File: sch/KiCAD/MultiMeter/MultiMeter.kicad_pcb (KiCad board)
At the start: 2 copper layers, 31.1 x 40.6 mm, 17 parts

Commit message: 回路図データ修正
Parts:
- removed Boost, OilPress: PinHeader_1x03_P2.54mm_Vertical, Connector_PinHeader_2.54mm:PinHeader_1x03_P2.54mm_Vertical
- removed OilTemp, WaterTemp: PinHeader_1x02_P2.54mm_Vertical, Connector_PinHeader_2.54mm:PinHeader_1x02_P2.54mm_Vertical
- removed Speed, Tacho: Pin_D1.2mm_L11.3mm_W3.0mm_Flat, Connector_Pin:Pin_D1.2mm_L11.3mm_W3.0mm_Flat
- added J1: Conn_01x02_Male, Connector_Molex:Molex_SPOX_5267-02A_1x02_P2.50mm_Vertical, F.Cu at (64.4, 65.4)
- added J2: Conn_01x02_Male, Connector_Molex:Molex_SPOX_5267-02A_1x02_P2.50mm_Vertical, F.Cu at (64.4, 56.5)
- added J3: Conn_01x03_Male, Connector_Molex:Molex_SPOX_5267-03A_1x03_P2.50mm_Vertical, F.Cu at (64.4, 45.1)
- added J4: Conn_01x03_Male, Connector_Molex:Molex_SPOX_5267-03A_1x03_P2.50mm_Vertical, F.Cu at (64.4, 33.7)
- added J5: Conn_01x02_Female, Connector_Molex:Molex_KK-254_AE-6410-02A_1x02_P2.54mm_Vertical, F.Cu at (64.8, 26.0)
- A1: value Arduino_Nano -> Arduino_Nano_v3.x
- C1, C2: value C_Rect_L4.6mm_W2.0mm_P2.50mm_MKS02_FKP02 -> C
- D1, D2, D3, D4: value D_T-1_P10.16mm_Horizontal -> 1N4148; footprint Diode_THT:D_T-1_P10.16mm_Horizontal -> Diode_THT:D_DO-35_SOD27_P7.62mm_Horizontal
- R1, R2, R3, R4: value R_Axial_DIN0207_L6.3mm_D2.5mm_P10.16mm_Horizontal -> R; footprint Resistor_THT:R_Axial_DIN0207_L6.3mm_D2.5mm_P10.16mm_Horizontal -> Resistor_THT:R_Axial_DIN0204_L3.6mm_D1.6mm_P7.62mm_Horizontal
- moved A1 55.7 mm to (42.5, 26.0), turned to 0 degrees
- moved R3 47.7 mm to (46.4, 25.4), turned to 0 degrees
- moved R4 40.3 mm to (46.4, 27.9), turned to 0 degrees
- moved D2 34.6 mm to (48.9, 38.1)
- moved C1 34.3 mm to (45.7, 55.2), turned to 0 degrees
- moved C2 34.1 mm to (52.1, 55.2)
- moved D1 29.9 mm to (48.9, 48.9), turned to 90 degrees
- moved D3 29.0 mm to (53.3, 48.9), turned to 90 degrees
- moved R1 23.8 mm to (54.0, 61.6), turned to 180 degrees
- moved D4 22.7 mm to (53.3, 38.1)
- moved R2 17.2 mm to (54.0, 59.1), turned to 180 degrees
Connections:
- A1 pad 1: (no net) -> unconnected-(A1-Pad1)
- A1 pad 10: (no net) -> unconnected-(A1-Pad10)
- A1 pad 11: (no net) -> unconnected-(A1-Pad11)
- A1 pad 12: (no net) -> unconnected-(A1-Pad12)
- A1 pad 13: (no net) -> unconnected-(A1-Pad13)
- A1 pad 14: (no net) -> unconnected-(A1-Pad14)
- A1 pad 15: (no net) -> unconnected-(A1-Pad15)
- A1 pad 16: (no net) -> unconnected-(A1-Pad16)
- A1 pad 17: (no net) -> unconnected-(A1-Pad17)
- A1 pad 18: (no net) -> unconnected-(A1-Pad18)
- A1 pad 19: (no net) -> unconnected-(A1-Pad19)
- A1 pad 2: (no net) -> unconnected-(A1-Pad2)
- A1 pad 20: (no net) -> Net-(A1-Pad20)
- A1 pad 21: (no net) -> Net-(A1-Pad21)
- A1 pad 22: (no net) -> Net-(A1-Pad22)
- A1 pad 23: (no net) -> Net-(A1-Pad23)
- A1 pad 24: (no net) -> unconnected-(A1-Pad24)
- A1 pad 25: (no net) -> unconnected-(A1-Pad25)
- A1 pad 26: (no net) -> unconnected-(A1-Pad26)
- A1 pad 27: (no net) -> Net-(A1-Pad27)
- A1 pad 28: (no net) -> unconnected-(A1-Pad28)
- A1 pad 29: (no net) -> Net-(A1-Pad29)
- A1 pad 3: (no net) -> unconnected-(A1-Pad3)
- A1 pad 30: (no net) -> unconnected-(A1-Pad30)
- A1 pad 4: (no net) -> Net-(A1-Pad29)
- A1 pad 5: (no net) -> Net-(A1-Pad5)
- A1 pad 6: (no net) -> Net-(A1-Pad6)
- A1 pad 7: (no net) -> unconnected-(A1-Pad7)
- A1 pad 8: (no net) -> unconnected-(A1-Pad8)
- A1 pad 9: (no net) -> unconnected-(A1-Pad9)
- C1 pad 1: (no net) -> Net-(A1-Pad5)
- C1 pad 2: (no net) -> Net-(A1-Pad29)
- C2 pad 1: (no net) -> Net-(A1-Pad6)
- C2 pad 2: (no net) -> Net-(A1-Pad29)
- D1 pad 1: (no net) -> Net-(A1-Pad5)
- D1 pad 2: (no net) -> Net-(A1-Pad29)
- D2 pad 1: (no net) -> Net-(A1-Pad27)
- D2 pad 2: (no net) -> Net-(A1-Pad5)
- D3 pad 1: (no net) -> Net-(A1-Pad6)
- D3 pad 2: (no net) -> Net-(A1-Pad29)
- D4 pad 1: (no net) -> Net-(A1-Pad27)
- D4 pad 2: (no net) -> Net-(A1-Pad6)
- R1 pad 1: (no net) -> Net-(A1-Pad20)
- R1 pad 2: (no net) -> Net-(A1-Pad29)
- R2 pad 1: (no net) -> Net-(A1-Pad21)
- R2 pad 2: (no net) -> Net-(A1-Pad29)
- R3 pad 1: (no net) -> Net-(A1-Pad5)
- R3 pad 2: (no net) -> Net-(J5-Pad1)
- R4 pad 1: (no net) -> Net-(A1-Pad6)
- R4 pad 2: (no net) -> Net-(J5-Pad2)
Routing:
- net (no net): track 290.2 -> 0.00 mm
- net Net-(A1-Pad29): track 0.00 -> 86.6 mm
- net Net-(A1-Pad27): track 0.00 -> 59.7 mm
- net Net-(A1-Pad6): track 0.00 -> 54.2 mm
- net Net-(A1-Pad5): track 0.00 -> 42.7 mm
- net Net-(A1-Pad20): track 0.00 -> 29.8 mm
- net Net-(A1-Pad21): track 0.00 -> 24.1 mm
- net Net-(A1-Pad23): track 0.00 -> 13.5 mm
- net Net-(J5-Pad1): track 0.00 -> 11.6 mm
- net Net-(J5-Pad2): track 0.00 -> 11.4 mm
- net Net-(A1-Pad22): track 0.00 -> 7.16 mm
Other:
- board size 31.1 x 40.6 mm -> 29.8 x 52.7 mm
- board text added: "2022/09/13"
- board text added: "Boost"
- board text added: "Oil.P"
- board text added: "Oil.T"
- board text added: "Water"
- board text removed: "2022/08/18"
- board text removed: "USB"

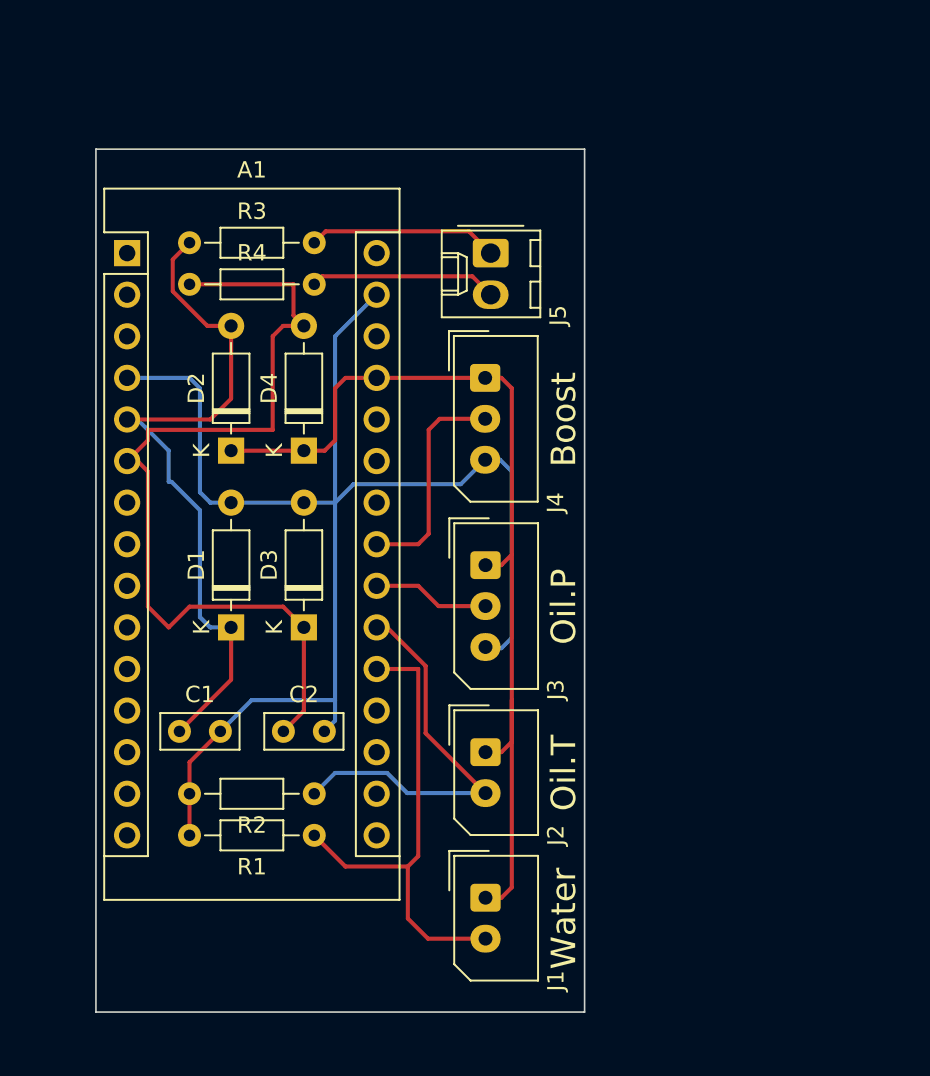
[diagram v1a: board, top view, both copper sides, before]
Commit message: デバック用PADを追加
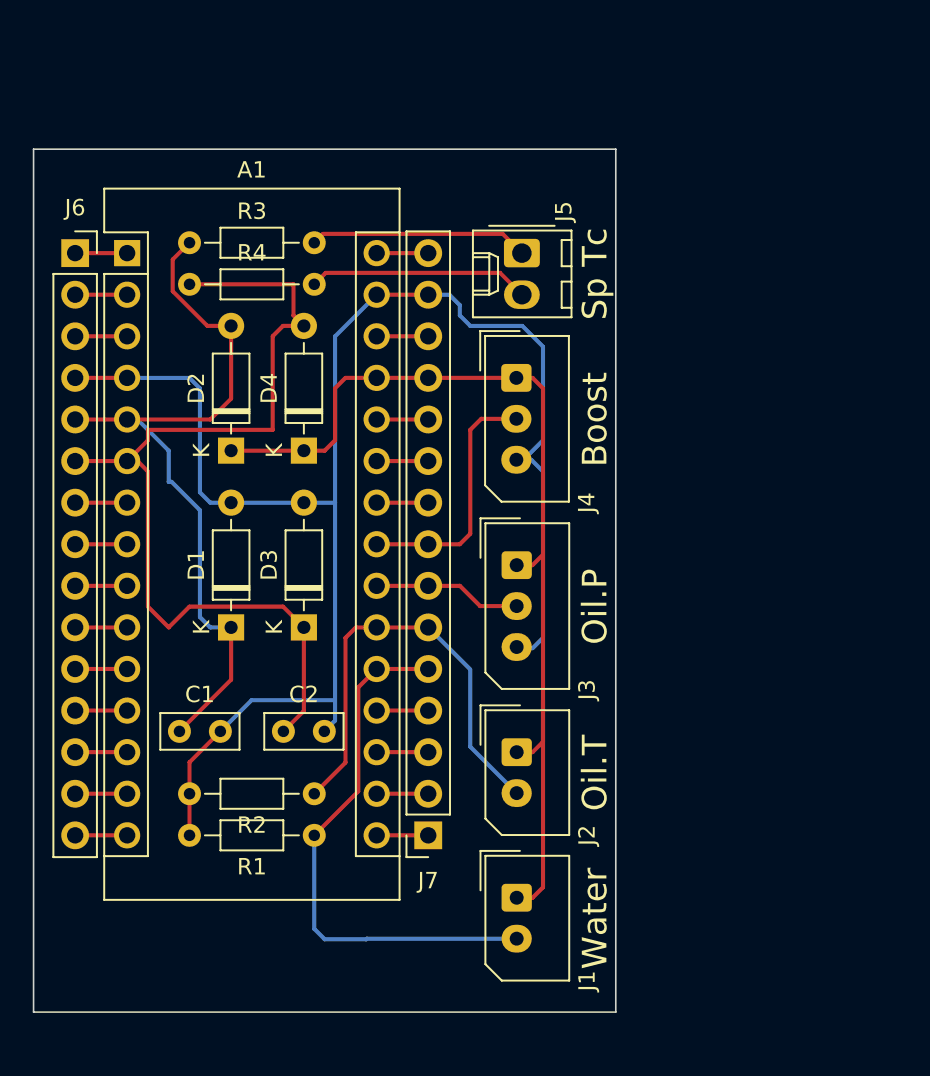
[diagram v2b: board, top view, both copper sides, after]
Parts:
- added J6: Conn_01x15, Connector_PinSocket_2.54mm:PinSocket_1x15_P2.54mm_Vertical, F.Cu at (39.4, 26.0)
- added J7: Conn_01x15, Connector_PinSocket_2.54mm:PinSocket_1x15_P2.54mm_Vertical, F.Cu at (60.9, 61.6)
- moved J1 1.91 mm to (66.3, 65.4)
- moved J2 1.91 mm to (66.3, 56.5)
- moved J3 1.91 mm to (66.3, 45.1)
- moved J4 1.91 mm to (66.3, 33.7)
- moved J5 1.91 mm to (66.7, 26.0)
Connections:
- A1 pad 1: unconnected-(A1-Pad1) -> Net-(A1-Pad1)
- A1 pad 10: unconnected-(A1-Pad10) -> Net-(A1-Pad10)
- A1 pad 11: unconnected-(A1-Pad11) -> Net-(A1-Pad11)
- A1 pad 12: unconnected-(A1-Pad12) -> Net-(A1-Pad12)
- A1 pad 13: unconnected-(A1-Pad13) -> Net-(A1-Pad13)
- A1 pad 14: unconnected-(A1-Pad14) -> Net-(A1-Pad14)
- A1 pad 15: unconnected-(A1-Pad15) -> Net-(A1-Pad15)
- A1 pad 16: unconnected-(A1-Pad16) -> Net-(A1-Pad16)
- A1 pad 17: unconnected-(A1-Pad17) -> Net-(A1-Pad17)
- A1 pad 18: unconnected-(A1-Pad18) -> Net-(A1-Pad18)
- A1 pad 19: unconnected-(A1-Pad19) -> Net-(A1-Pad19)
- A1 pad 2: unconnected-(A1-Pad2) -> Net-(A1-Pad2)
- A1 pad 24: unconnected-(A1-Pad24) -> Net-(A1-Pad24)
- A1 pad 25: unconnected-(A1-Pad25) -> Net-(A1-Pad25)
- A1 pad 26: unconnected-(A1-Pad26) -> Net-(A1-Pad26)
- A1 pad 28: unconnected-(A1-Pad28) -> Net-(A1-Pad28)
- A1 pad 3: unconnected-(A1-Pad3) -> Net-(A1-Pad3)
- A1 pad 30: unconnected-(A1-Pad30) -> Net-(A1-Pad30)
- A1 pad 7: unconnected-(A1-Pad7) -> Net-(A1-Pad7)
- A1 pad 8: unconnected-(A1-Pad8) -> Net-(A1-Pad8)
- A1 pad 9: unconnected-(A1-Pad9) -> Net-(A1-Pad9)
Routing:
- net Net-(A1-Pad29): track 86.6 -> 99.2 mm
- net Net-(A1-Pad21): track 24.1 -> 28.0 mm
- net Net-(A1-Pad20): track 29.8 -> 33.2 mm
- net Net-(A1-Pad6): track 54.2 -> 57.4 mm
- net Net-(A1-Pad5): track 42.7 -> 45.9 mm
- net Net-(A1-Pad9): track 0.00 -> 3.18 mm
- net Net-(A1-Pad8): track 0.00 -> 3.18 mm
- net Net-(A1-Pad7): track 0.00 -> 3.18 mm
- net Net-(A1-Pad3): track 0.00 -> 3.18 mm
- net Net-(A1-Pad2): track 0.00 -> 3.18 mm
- net Net-(A1-Pad15): track 0.00 -> 3.18 mm
- net Net-(A1-Pad14): track 0.00 -> 3.18 mm
- net Net-(A1-Pad13): track 0.00 -> 3.18 mm
- net Net-(A1-Pad12): track 0.00 -> 3.18 mm
- net Net-(A1-Pad11): track 0.00 -> 3.18 mm
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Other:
- board size 29.8 x 52.7 mm -> 35.6 x 52.7 mm
- board text added: "Sp Tc"

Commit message: 確認用LEDを追加
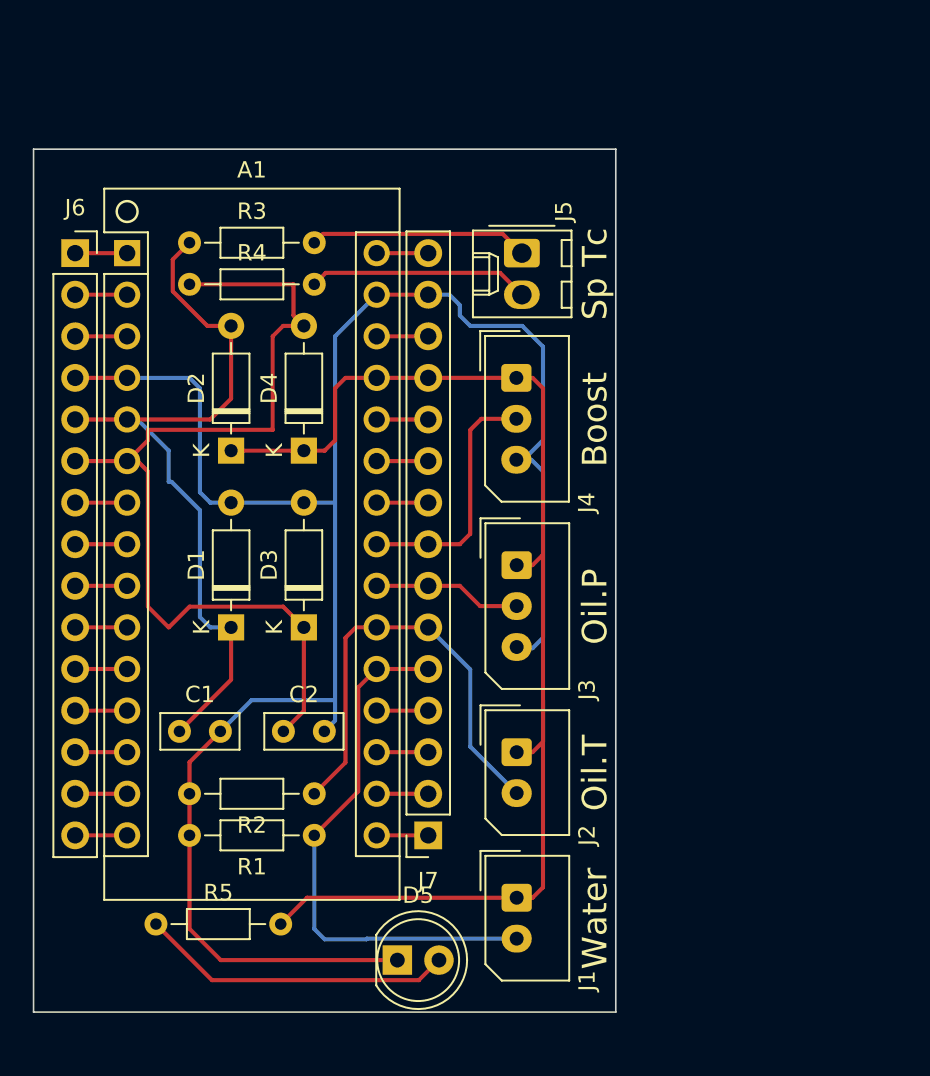
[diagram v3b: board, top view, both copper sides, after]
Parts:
- added D5: CQY99, LED_THT:LED_D5.0mm_IRGrey, F.Cu at (59.0, 69.2)
- added R5: R, Resistor_THT:R_Axial_DIN0204_L3.6mm_D1.6mm_P7.62mm_Horizontal, F.Cu at (44.3, 67.0)
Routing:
- net Net-(D5-Pad2): track 0.00 -> 19.2 mm
- net Net-(A1-Pad29): track 99.2 -> 118.4 mm
- net Net-(A1-Pad27): track 61.6 -> 76.7 mm
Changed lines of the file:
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@@
   (net 30 "Net-(J5-Pad1)")
   (net 31 "Net-(J5-Pad2)")
+  (net 32 "Net-(D5-Pad2)")
   (footprint "Module:Arduino_Nano" (layer "F.Cu")
     (at 42.545 26.035)
@@
     )
   )
+  (footprint "LED_THT:LED_D5.0mm_IRGrey" (layer "F.Cu")
+    (at 59.05 69.215)
+    (descr "LED, diameter 5.0mm, 2 pins, http://cdn-reichelt.de/documents/datenblatt/A500/LL-504BC2E-009.pdf")
+    (tags "LED diameter 5.0mm 2 pins")
+    (property "Sheetfile" "MultiMeter.kicad_sch")
+    (property "Sheetname" "")
+    (attr through_hole)
+    (fp_text reference "D5" (at 1.27 -3.96) (layer "F.SilkS")
+      (effects (font (size 1 1) (thickness 0.15)))
+    )
+    (fp_text value "CQY99" (at 1.27 3.96) (layer "F.Fab")
+      (effects (font (size 1 1) (thickness 0.15)))
+    )
+    (fp_text user "${REFERENCE}" (at 1.25 0) (layer "F.Fab")
+      (effects (font (size 0.8 0.8) (thickness 0.2)))
+    )
+    (fp_line (start -1.29 -1.545) (end -1.29 1.545) (layer "F.SilkS") (width 0.12))
+    (fp_arc (start 4.26 -0.000462) (mid 2.072002 2.880433) (end -1.29 1.54483) (layer "F.SilkS") (width 0.12))
+    (fp_arc (start -1.29 -1.54483) (mid 2.072002 -2.880433) (end 4.26 0.000462) (layer "F.SilkS") (width 0.12))
+    (fp_circle (center 1.27 0) (end 3.77 0) (layer "F.SilkS") (width 0.12) (fill none))
+    (fp_line (start -1.95 -3.25) (end -1.95 3.25) (layer "F.CrtYd") (width 0.05))
+    (fp_line (start 4.5 3.25) (end 4.5 -3.25) (layer "F.CrtYd") (width 0.05))
+    (fp_line (start -1.95 3.25) (end 4.5 3.25) (layer "F.CrtYd") (width 0.05))
+    (fp_line (start 4.5 -3.25) (end -1.95 -3.25) (layer "F.CrtYd") (width 0.05))
+    (fp_line (start -1.23 -1.469694) (end -1.23 1.469694) (layer "F.Fab") (width 0.1))
+    (fp_arc (start -1.23 -1.469694) (mid 4.17 0.000016) (end -1.230016 1.469666) (layer "F.Fab") (width 0.1))
+    (fp_circle (center 1.27 0) (end 3.77 0) (layer "F.Fab") (width 0.1) (fill none))
+    (pad "1" thru_hole rect (at 0 0) (size 1.8 1.8) (drill 0.9) (layers *.Cu *.Mask)
+      (net 4 "Net-(A1-Pad29)") (pinfunction "K") (pintype "passive"))
+    (pad "2" thru_hole circle (at 2.54 0) (size 1.8 1.8) (drill 0.9) (layers *.Cu *.Mask)
+      (net 32 "Net-(D5-Pad2)") (pinfunction "A") (pintype "passive"))
+    (model "${KICAD6_3DMODEL_DIR}/LED_THT.3dshapes/LED_D5.0mm_IRGrey.wrl"
+      (offset (xyz 0 0 0))
+      (scale (xyz 1 1 1))
+      (rotate (xyz 0 0 0))
+    )
+  )
   (footprint "Diode_THT:D_DO-35_SOD27_P7.62mm_Horizontal" (layer "F.Cu")
     (at 53.34 48.895 90)
@@
     )
   )
+  (footprint "Resistor_THT:R_Axial_DIN0204_L3.6mm_D1.6mm_P7.62mm_Horizontal" (layer "F.Cu")
+    (at 44.305 67.015)
+    (descr "Resistor, Axial_DIN0204 series, Axial, Horizontal, pin pitch=7.62mm, 0.167W, length*diameter=3.6*1.6mm^2, http://cdn-reichelt.de/documents/datenblatt/B400/1_4W%23YAG.pdf")
+    (tags "Resistor Axial_DIN0204 series Axial Horizontal pin pitch 7.62mm 0.167W length 3.6mm diameter 1.6mm")
+    (property "Sheetfile" "MultiMeter.kicad_sch")
+    (property "Sheetname" "")
+    (attr through_hole)
+    (fp_text reference "R5" (at 3.81 -1.92) (layer "F.SilkS")
+      (effects (font (size 1 1) (thickness 0.15)))
+    )
+    (fp_text value "R" (at 3.81 1.92) (layer "F.Fab")
+      (effects (font (size 1 1) (thickness 0.15)))
+    )
+    (fp_text user "${REFERENCE}" (at 3.81 0) (layer "F.Fab")
+      (effects (font (size 0.72 0.72) (thickness 0.108)))
+    )
+    (fp_line (start 5.73 0.92) (end 5.73 -0.92) (layer "F.SilkS") (width 0.12))
+    (fp_line (start 6.68 0) (end 5.73 0) (layer "F.SilkS") (width 0.12))
+    (fp_line (start 1.89 -0.92) (end 1.89 0.92) (layer "F.SilkS") (width 0.12))
+    (fp_line (start 1.89 0.92) (end 5.73 0.92) (layer "F.SilkS") (width 0.12))
+    (fp_line (start 0.94 0) (end 1.89 0) (layer "F.SilkS") (width 0.12))
+    (fp_line (start 5.73 -0.92) (end 1.89 -0.92) (layer "F.SilkS") (width 0.12))
+    (fp_line (start 8.57 1.05) (end 8.57 -1.05) (layer "F.CrtYd") (width 0.05))
+    (fp_line (start -0.95 -1.05) (end -0.95 1.05) (layer "F.CrtYd") (width 0.05))
+    (fp_line (start -0.95 1.05) (end 8.57 1.05) (layer "F.CrtYd") (width 0.05))
+    (fp_line (start 8.57 -1.05) (end -0.95 -1.05) (layer "F.CrtYd") (width 0.05))
+    (fp_line (start 5.61 0.8) (end 5.61 -0.8) (layer "F.Fab") (width 0.1))
+    (fp_line (start 2.01 -0.8) (end 2.01 0.8) (layer "F.Fab") (width 0.1))
+    (fp_line (start 0 0) (end 2.01 0) (layer "F.Fab") (width 0.1))
+    (fp_line (start 7.62 0) (end 5.61 0) (layer "F.Fab") (width 0.1))
+    (fp_line (start 5.61 -0.8) (end 2.01 -0.8) (layer "F.Fab") (width 0.1))
+    (fp_line (start 2.01 0.8) (end 5.61 0.8) (layer "F.Fab") (width 0.1))
+    (pad "1" thru_hole circle (at 0 0) (size 1.4 1.4) (drill 0.7) (layers *.Cu *.Mask)
+      (net 32 "Net-(D5-Pad2)") (pintype "passive"))
+    (pad "2" thru_hole oval (at 7.62 0) (size 1.4 1.4) (drill 0.7) (layers *.Cu *.Mask)
+      (net 27 "Net-(A1-Pad27)") (pintype "passive"))
+    (model "${KICAD6_3DMODEL_DIR}/Resistor_THT.3dshapes/R_Axial_DIN0204_L3.6mm_D1.6mm_P7.62mm_Horizontal.wrl"
+      (offset (xyz 0 0 0))
+      (scale (xyz 1 1 1))
+      (rotate (xyz 0 0 0))
+    )
+  )
   (footprint "Connector_Molex:Molex_SPOX_5267-03A_1x03_P2.50mm_Vertical" (layer "F.Cu")
     (at 66.3175 33.655 -90)
@@
     )
   )
+  (gr_circle (center 42.545 23.495) (end 43.18 23.495) (layer "F.SilkS") (width 0.15) (fill none))
   (gr_rect (start 72.39 72.39) (end 36.83 19.685) (layer "Edge.Cuts") (width 0.1) (fill none))
   (gr_text "2022/09/13" (at 45.72 71.12) (layer "B.SilkS")
@@
   (segment (start 42.545 28.575) (end 39.37 28.575) (width 0.25) (layer "F.Cu") (net 2))
   (segment (start 42.545 31.115) (end 39.37 31.115) (width 0.25) (layer "F.Cu") (net 3))
+  (segment (start 48.26 69.215) (end 59.05 69.215) (width 0.25) (layer "F.Cu") (net 4))
   (segment (start 57.785 28.575) (end 60.935 28.575) (width 0.25) (layer "F.Cu") (net 4))
   (segment (start 46.355 57.13) (end 48.24 55.245) (width 0.25) (layer "F.Cu") (net 4))
@@
   (segment (start 46.355 59.055) (end 46.355 57.13) (width 0.25) (layer "F.Cu") (net 4))
   (segment (start 42.545 33.655) (end 39.37 33.655) (width 0.25) (layer "F.Cu") (net 4))
+  (segment (start 46.355 67.31) (end 48.26 69.215) (width 0.25) (layer "F.Cu") (net 4))
+  (segment (start 46.355 61.595) (end 46.355 67.31) (width 0.25) (layer "F.Cu") (net 4))
   (segment (start 57.785 28.575) (end 55.245 31.115) (width 0.25) (layer "B.Cu") (net 4))
   (segment (start 48.24 55.245) (end 50.145 53.34) (width 0.25) (layer "B.Cu") (net 4))
@@
   (segment (start 57.785 38.735) (end 60.935 38.735) (width 0.25) (layer "F.Cu") (net 25))
   (segment (start 57.785 36.195) (end 60.935 36.195) (width 0.25) (layer "F.Cu") (net 26))
+  (segment (start 66.3375 65.405) (end 53.535 65.405) (width 0.25) (layer "F.Cu") (net 27))
   (segment (start 55.245 34.29) (end 55.245 37.465) (width 0.25) (layer "F.Cu") (net 27))
   (segment (start 67.3025 45.0925) (end 67.945 44.45) (width 0.25) (layer "F.Cu") (net 27))
@@
   (segment (start 67.31 33.655) (end 66.3175 33.655) (width 0.25) (layer "F.Cu") (net 27))
   (segment (start 66.3375 56.515) (end 67.31 56.515) (width 0.25) (layer "F.Cu") (net 27))
+  (segment (start 53.535 65.405) (end 51.925 67.015) (width 0.25) (layer "F.Cu") (net 27))
   (segment (start 57.785 33.655) (end 55.88 33.655) (width 0.25) (layer "F.Cu") (net 27))
   (segment (start 67.945 53.34) (end 67.945 44.45) (width 0.25) (layer "F.Cu") (net 27))
@@
   (segment (start 65.32 27.24) (end 66.655 28.575) (width 0.25) (layer "F.Cu") (net 31))
   (segment (start 54.675 27.24) (end 65.32 27.24) (width 0.25) (layer "F.Cu") (net 31))
+  (segment (start 60.365489 70.439511) (end 47.729511 70.439511) (width 0.25) (layer "F.Cu") (net 32))
+  (segment (start 61.59 69.215) (end 60.365489 70.439511) (width 0.25) (layer "F.Cu") (net 32))
+  (segment (start 47.729511 70.439511) (end 44.305 67.015) (width 0.25) (layer "F.Cu") (net 32))
 )

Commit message: 微修正
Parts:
- R5: value R -> 200 ohm
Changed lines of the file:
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@@
       (effects (font (size 1 1) (thickness 0.15)))
     )
-    (fp_text value "R" (at 3.81 1.92) (layer "F.Fab")
+    (fp_text value "200 ohm" (at 3.81 1.92) (layer "F.Fab")
       (effects (font (size 1 1) (thickness 0.15)))
     )
